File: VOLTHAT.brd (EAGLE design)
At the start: 64 x 56 mm, 25 parts, among them IC2 EUP3476SO08T, J1 DC IN

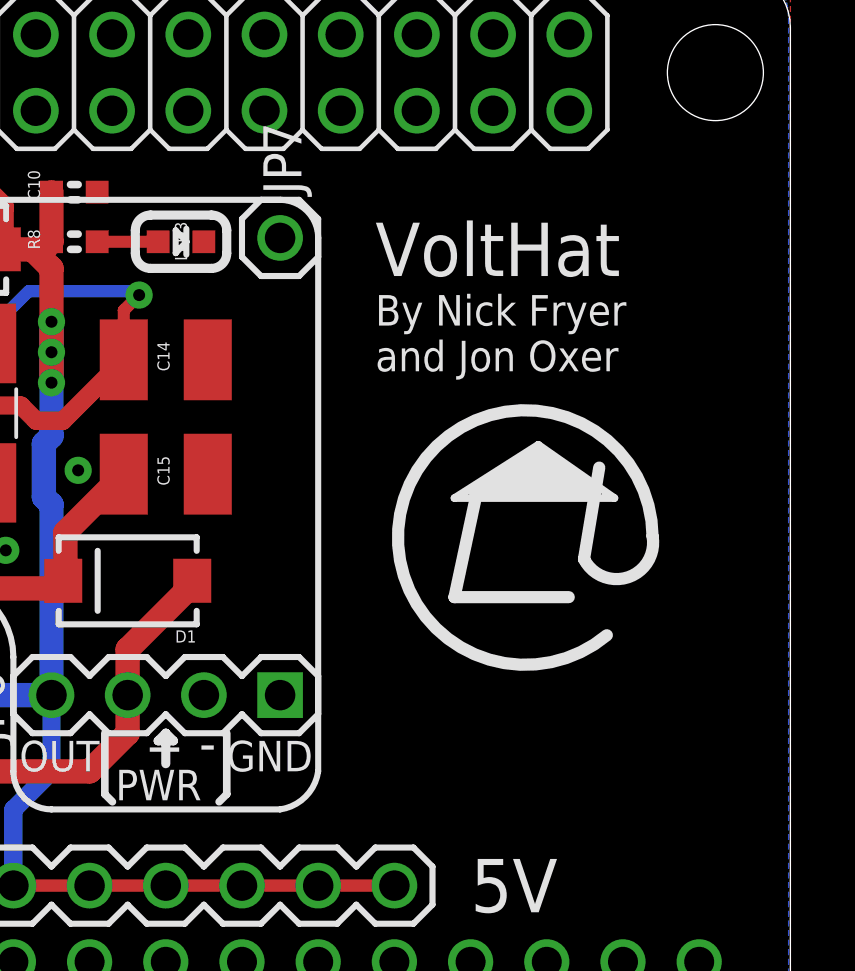
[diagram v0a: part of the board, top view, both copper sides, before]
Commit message: Added header to take power from PoE on Raspberry Pi 3 B+
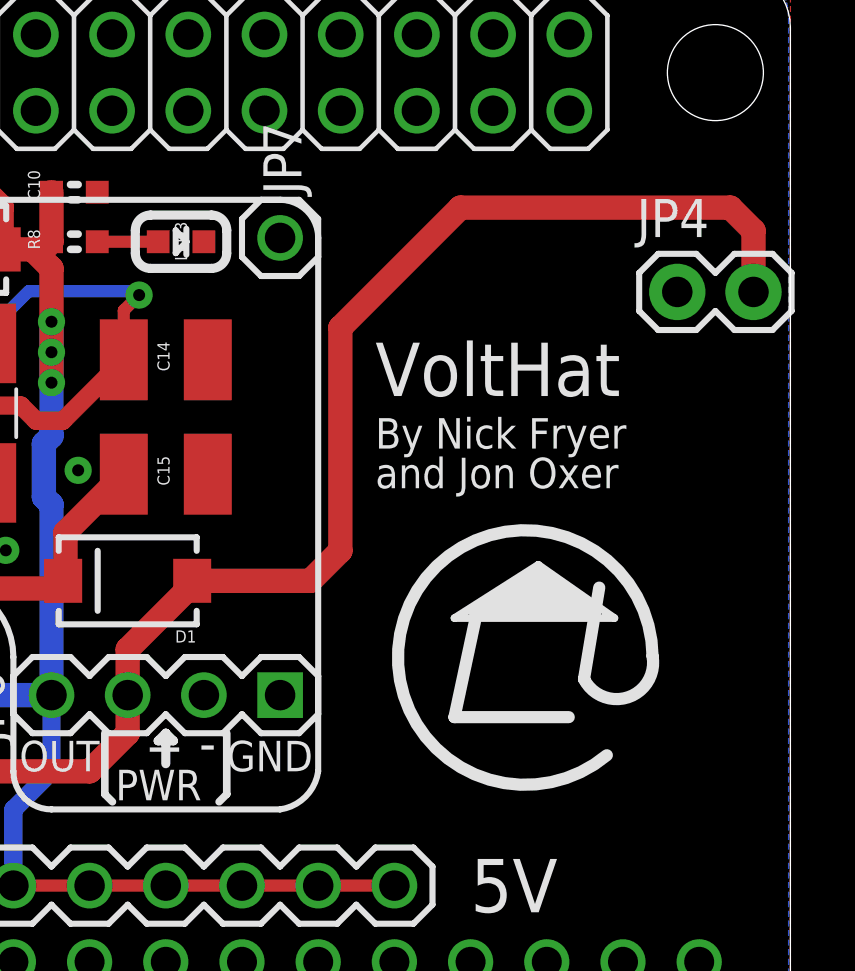
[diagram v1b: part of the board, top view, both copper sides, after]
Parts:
- added JP4: (no value), freetronics-jon:1X02
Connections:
- net GND: now also JP4.1
- net POS: now also JP4.2
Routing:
- net POS: track 49.6 -> 80.2 mm
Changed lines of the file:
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@@
 <setting verticaltext="up"/>
 </settings>
-<grid distance="0.025" unitdist="inch" unit="inch" style="lines" multiple="1" display="yes" altdistance="3.125" altunitdist="mil" altunit="mil"/>
+<grid distance="1" unitdist="mm" unit="mm" style="lines" multiple="1" display="yes" altdistance="3.125" altunitdist="mil" altunit="mil"/>
 <layers>
 <layer number="1" name="Top" color="12" fill="1" visible="yes" active="yes"/>
@@
 <text x="53.34" y="5.08" size="1.778" layer="21" font="vector" ratio="15" align="center-left">GND</text>
 <text x="5.842" y="5.08" size="1.778" layer="21" font="vector" ratio="15" align="center-left">GND</text>
-<text x="50.165" y="45.72" size="1.778" layer="21" font="vector" ratio="15">VoltHat</text>
-<text x="50.165" y="43.815" size="1.016" layer="21" font="vector" ratio="15" align="center-left">By Nick Fryer
+<text x="50.165" y="41.72" size="1.778" layer="21" font="vector" ratio="15">VoltHat</text>
+<text x="50.165" y="39.815" size="1.016" layer="21" font="vector" ratio="15" distance="30" align="center-left">By Nick Fryer
 and Jon Oxer</text>
 <hole x="3.5" y="3.5" drill="3.2"/>
@@
 <wire x1="16.891" y1="29.845" x2="17.653" y2="29.845" width="0.3048" layer="21"/>
 <text x="12.7" y="31.75" size="1.778" layer="21" font="vector" ratio="18">2.1mm</text>
-<wire x1="59.406" y1="37.048" x2="57.882" y2="33.746" width="0.4064" layer="21" curve="309.2564"/>
-<wire x1="59.406" y1="37.048" x2="57.12" y2="36.286" width="0.4064" layer="21" curve="-163.361194"/>
-<wire x1="57.12" y1="36.286" x2="57.628" y2="39.334" width="0.4064" layer="21"/>
-<wire x1="56.612" y1="35.016" x2="52.802" y2="35.016" width="0.4064" layer="21"/>
-<wire x1="52.802" y1="35.016" x2="53.564" y2="38.572" width="0.4064" layer="21"/>
-<wire x1="58.136" y1="38.318" x2="52.802" y2="38.318" width="0.254" layer="21"/>
-<wire x1="52.802" y1="38.318" x2="55.596" y2="40.096" width="0.254" layer="21"/>
-<wire x1="55.596" y1="40.096" x2="58.136" y2="38.318" width="0.254" layer="21"/>
-<wire x1="53.31" y1="38.572" x2="53.564" y2="38.572" width="0.254" layer="21"/>
-<wire x1="53.564" y1="38.572" x2="57.374" y2="38.572" width="0.254" layer="21"/>
-<wire x1="57.374" y1="38.572" x2="55.596" y2="39.842" width="0.254" layer="21"/>
-<wire x1="55.596" y1="39.842" x2="53.564" y2="38.572" width="0.254" layer="21"/>
-<wire x1="56.866" y1="38.826" x2="54.072" y2="38.826" width="0.4064" layer="21"/>
-<wire x1="54.072" y1="38.826" x2="55.596" y2="39.588" width="0.4064" layer="21"/>
-<wire x1="55.596" y1="39.588" x2="56.358" y2="39.08" width="0.4064" layer="21"/>
-<wire x1="56.358" y1="39.08" x2="55.088" y2="39.08" width="0.4064" layer="21"/>
-<wire x1="55.088" y1="39.08" x2="55.596" y2="39.334" width="0.4064" layer="21"/>
+<wire x1="59.406" y1="33.048" x2="57.882" y2="29.746" width="0.4064" layer="21" curve="309.2564"/>
+<wire x1="59.406" y1="33.048" x2="57.12" y2="32.286" width="0.4064" layer="21" curve="-163.361194"/>
+<wire x1="57.12" y1="32.286" x2="57.628" y2="35.334" width="0.4064" layer="21"/>
+<wire x1="56.612" y1="31.016" x2="52.802" y2="31.016" width="0.4064" layer="21"/>
+<wire x1="52.802" y1="31.016" x2="53.564" y2="34.572" width="0.4064" layer="21"/>
+<wire x1="58.136" y1="34.318" x2="52.802" y2="34.318" width="0.254" layer="21"/>
+<wire x1="52.802" y1="34.318" x2="55.596" y2="36.096" width="0.254" layer="21"/>
+<wire x1="55.596" y1="36.096" x2="58.136" y2="34.318" width="0.254" layer="21"/>
+<wire x1="53.31" y1="34.572" x2="53.564" y2="34.572" width="0.254" layer="21"/>
+<wire x1="53.564" y1="34.572" x2="57.374" y2="34.572" width="0.254" layer="21"/>
+<wire x1="57.374" y1="34.572" x2="55.596" y2="35.842" width="0.254" layer="21"/>
+<wire x1="55.596" y1="35.842" x2="53.564" y2="34.572" width="0.254" layer="21"/>
+<wire x1="56.866" y1="34.826" x2="54.072" y2="34.826" width="0.4064" layer="21"/>
+<wire x1="54.072" y1="34.826" x2="55.596" y2="35.588" width="0.4064" layer="21"/>
+<wire x1="55.596" y1="35.588" x2="56.358" y2="35.08" width="0.4064" layer="21"/>
+<wire x1="56.358" y1="35.08" x2="55.088" y2="35.08" width="0.4064" layer="21"/>
+<wire x1="55.088" y1="35.08" x2="55.596" y2="35.334" width="0.4064" layer="21"/>
 </plain>
 <attributes>
@@
 <attribute name="VALUE" x="41.656" y="33.909" size="0.4064" layer="27" rot="R180"/>
 </element>
+<element name="JP4" library="freetronics-jon" library_urn="urn:adsk.eagle:library:7065448" package="1X02" package3d_urn="urn:adsk.eagle:package:7066393/1" value="" x="60.23" y="45.19" smashed="yes">
+<attribute name="NAME" x="58.8838" y="47.0188" size="1.27" layer="25" ratio="10"/>
+<attribute name="VALUE" x="58.96" y="42.015" size="1.27" layer="27"/>
+</element>
 </elements>
 <signals>
@@
 <via x="40.259" y="39.243" extent="1-16" drill="0.4"/>
 <contactref element="JP3" pad="1"/>
+<contactref element="JP4" pad="1"/>
 </signal>
 <signal name="5V">
@@
 <wire x1="10.922" y1="33.02" x2="10.922" y2="38.918" width="0.8128" layer="1"/>
 <wire x1="10.922" y1="38.918" x2="7.62" y2="42.22" width="0.8128" layer="1"/>
+<contactref element="JP4" pad="2"/>
+<wire x1="44.06" y1="35.56" x2="48" y2="35.56" width="0.8128" layer="1"/>
+<wire x1="48" y1="35.56" x2="49" y2="36.56" width="0.8128" layer="1"/>
+<wire x1="49" y1="44" x2="53" y2="48" width="0.8128" layer="1"/>
+<wire x1="53" y1="48" x2="62" y2="48" width="0.8128" layer="1"/>
+<wire x1="62" y1="48" x2="62.77" y2="47.23" width="0.8128" layer="1"/>
+<wire x1="62.77" y1="47.23" x2="62.77" y2="45.19" width="0.8128" layer="1"/>
+<wire x1="49" y1="36.56" x2="49" y2="44" width="0.8128" layer="1"/>
 </signal>
 <signal name="N$204">

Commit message: Major routing for v1.0 release
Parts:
- removed JP2: M16PTH, freetronics-jon:1X16
- added JP10: OLED, freetronics-jon:1X04
- added JP9: M14PTH, freetronics-jon:1X14
- added SJ1, SJ2: (no value), freetronics-jon:SJ
- JP1: value M16PTH -> M14PTH; device freetronics-jon:1X16 -> freetronics-jon:1X14
- moved JP1 21.7 mm to (20.3, 5.08)
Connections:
- new net 3.3V: JP10.3, U$2.1
- new net N$1: JP4.1, SJ2.1
- new net N$2: JP4.2, SJ1.1
- new net SCL: JP10.2, U$2.5
- new net SDA: JP10.1, U$2.3
- net 5V: now also JP9.1, JP9.10, JP9.11, JP9.12, JP9.13, JP9.14, JP9.2, JP9.3, JP9.4, JP9.5, JP9.6, JP9.7, JP9.8, JP9.9; no longer JP1.1, JP1.10, JP1.11, JP1.12, JP1.13, JP1.14, JP1.15, JP1.16, JP1.2, JP1.3, JP1.4, JP1.5, JP1.6, JP1.7, JP1.8, JP1.9
- net GND: now also JP1.1, JP1.10, JP1.11, JP1.12, JP1.13, JP1.14, JP1.2, JP1.3, JP1.4, JP1.5, JP1.6, JP1.7, JP1.8, JP1.9, JP10.4, SJ2.2, U$2.14, U$2.20, U$2.25, U$2.30, U$2.39, U$2.9; no longer JP2.1, JP2.10, JP2.11, JP2.12, JP2.13, JP2.14, JP2.15, JP2.16, JP2.2, JP2.3, JP2.4, JP2.5, JP2.6, JP2.7, JP2.8, JP2.9, JP4.1
- net POS: now also SJ1.2; no longer JP4.2
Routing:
- net 5V: track 159.8 -> 42.0 mm, vias 3 -> 0
- net 3.3V: track 0.00 -> 42.9 mm
- net SCL: track 0.00 -> 40.2 mm
- net SDA: track 0.00 -> 36.4 mm
- net POS: track 80.2 -> 69.9 mm
- net N$2: track 0.00 -> 9.37 mm
- net N$1: track 0.00 -> 4.55 mm
- net VFEED: track 32.4 -> 28.3 mm
- added copper zone on layer 16, net 5V
- removed copper zone on layer 16, net GND
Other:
- board text added: "3V3"
- board text added: "7-28V PoE"
- board text added: "Copyright 2019 SuperHouse Automation Pty Ltd Released under the terms of the TAPR Open Hardware License: www.tapr.org/OHL"
- board text added: "I2C"
- board text added: "SCL"
- board text added: "SDA"
- board text added: "Super House"

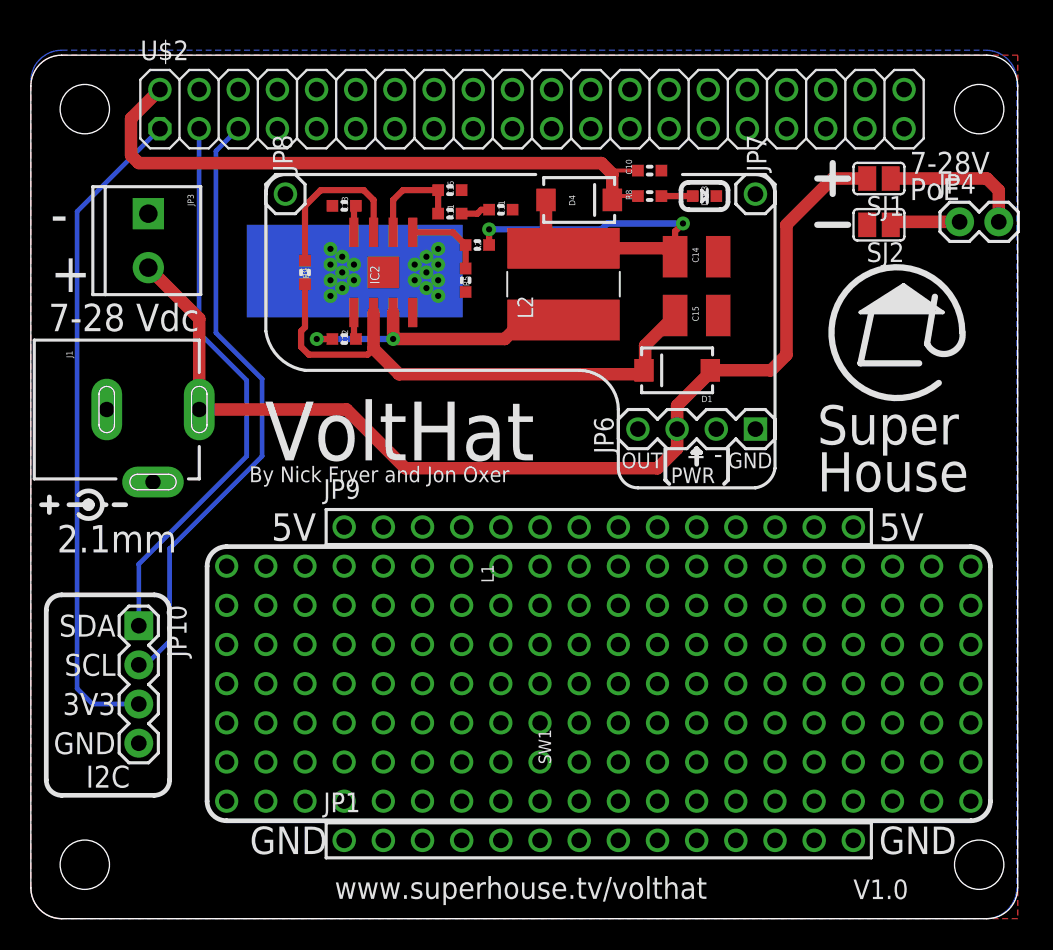
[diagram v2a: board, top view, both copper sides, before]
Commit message: Major rework with 3A regulator module for v2.0 release
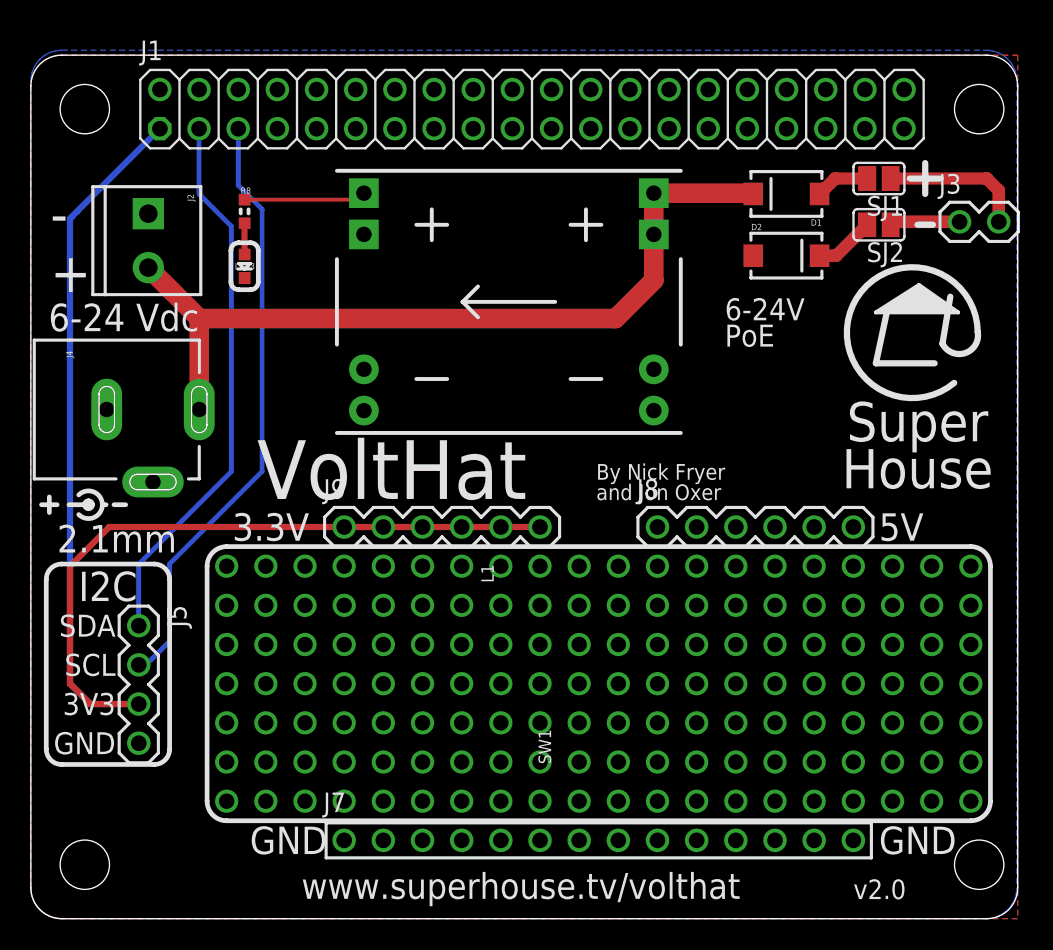
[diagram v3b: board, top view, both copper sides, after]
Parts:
- removed C10: 1uF 16V, freetronics:0603
- removed C11: 2.2nF 0603, freetronics-marc:0603
- removed C12: 10nF 50V, freetronics-marc:0603
- removed C13: 100nF, freetronics-marc:0603
- removed C14: 22uF 10V 1210 ceramic, freetronics-jon:C1210
- removed C15: 10uF 50V 1210 ceramic, freetronics-jon:C1210
- removed C16: 22pF NOT PLACED, freetronics-marc:0603
- removed D4: SK34A-LTP 3A 40V SCHOTTKY, freetronics-master-v1:SMA-DIODE
- removed IC2: EUP3476SO08T, freetronics-jon:SO08T
- removed JP10: OLED, freetronics-jon:1X04
- removed JP3: DC IN, freetronics-jon:SCREWTERMINAL-3.5MM-2
- removed JP4: (no value), freetronics-jon:1X02
- removed JP6: Pwr Header, freetronics:1X04
- removed JP7, JP8: (no value), freetronics:1X01
- removed JP9: M14PTH, freetronics-jon:1X14
- removed L2: CDRH6D38SMT, freetronics-jon:CDRH
- removed R11: 15K, freetronics-marc:0603
- removed R2: 57K 1%, freetronics-marc:0603
- removed R5: 10K 1%, freetronics-marc:0603
- removed R9: 100K, freetronics-marc:0603
- removed U$2: M40PTH, freetronics-jon:2X20
- added D2: SS56, SuperHouse-DiscreteSemi:SMA-DIODE
- added J2: DC IN, SuperHouse-Connectors:SCREWTERMINAL-3.5MM-2
- added J3: (no value), SuperHouse-Connectors:1X02-S-BELOW
- added J4: DC IN, SuperHouse-Connectors:POWER_JACK_SLOTS
- added J5: OLED, SuperHouse-Connectors:1X04
- added J8, J9: M06-PLAIN, SuperHouse-Connectors:1X06
- added VR1: DC5V3A-PTH, SuperHouse-Regulators:DC5V3A-PTH
- D1: value SK34A-LTP 3A 40V SCHOTTKY -> SS56; device freetronics-master-v1:SMA-DIODE -> SuperHouse-DiscreteSemi:SMA-DIODE
- J1: value DC IN -> M40-SOCKET-BELOW; device freetronics-jon:POWER_JACK_PTH_SLOTS -> SuperHouse-Connectors:2X20-S-BELOW
- LED3: device freetronics:LED-0603 -> SuperHouse-LEDs:LED-0603
- R8: device freetronics:0603 -> SuperHouse-DiscreteSemi:R0603
- moved LED3 30.2 mm to (13.9, 42.3), turned to 270 degrees
- moved R8 26.3 mm to (13.9, 45.9), turned to 270 degrees
- moved J1 21.4 mm to (8.37, 51.2), turned to 0 degrees
- moved D1 13.5 mm to (49.0, 47.0)
- renumbered JP1 to J7
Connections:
- removed net N$204: IC2.7, R9.1
- removed net N$205: IC2.5, R2.2, R5.2
- removed net N$206: C16.1, IC2.6, R11.2
- removed net N$207: C11.1, R11.1
- removed net N$208: C12.2, IC2.1
- removed net N$209: C13.2, IC2.8
- removed net N$210: C12.1, IC2.3, L2.1
- removed net VFEED: C14.1, D4.A, L2.2, R2.1
- removed net VIN: C15.1, D1.C, IC2.2, R9.2
- new net N$24: D1.A, SJ1.2
- new net N$25: D2.C, SJ2.2
- net 3.3V: now also J1.1, J5.3, J9.1, J9.2, J9.3, J9.4, J9.5, J9.6; no longer JP10.3, U$2.1
- net 5V: now also J1.2, J1.4, J8.1, J8.2, J8.3, J8.4, J8.5, J8.6, VR1.3A, VR1.3B; no longer C10.1, D4.C, JP6.4, JP9.1, JP9.10, JP9.11, JP9.12, JP9.13, JP9.14, JP9.2, JP9.3, JP9.4, JP9.5, JP9.6, JP9.7, JP9.8, JP9.9, U$2.2, U$2.4
- net GND: now also D2.A, J1.14, J1.20, J1.25, J1.30, J1.39, J1.6, J1.9, J2.1, J4.GND, J4.GNDBREAK, J5.4, VR1.1A, VR1.1B, VR1.4A, VR1.4B; no longer C10.2, C11.2, C13.1, C14.2, C15.2, C16.2, IC2.4, IC2.9, J1.GND, J1.GNDBREAK, JP10.4, JP3.1, JP6.1, JP6.2, JP7.1, R5.1, SJ2.2, U$2.14, U$2.20, U$2.25, U$2.30, U$2.39, U$2.6, U$2.9
- net N$1: now also J3.1; no longer JP4.1
- net N$2: now also J3.2; no longer JP4.2
- net POS: now also D1.C, J2.2, J4.PWR, VR1.2A, VR1.2B; no longer D1.A, J1.PWR, JP3.2, JP6.3, SJ1.2
- net SCL: now also J1.5, J5.2; no longer JP10.2, U$2.5
- net SDA: now also J1.3, J5.1; no longer JP10.1, U$2.3
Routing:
- net 3.3V: track 42.9 -> 87.6 mm
- net VIN: track 34.3 -> 0.00 mm
- net 5V: track 42.0 -> 7.84 mm
- net VFEED: track 28.3 -> 0.00 mm, vias 2 -> 0
- net N$210: track 19.4 -> 0.00 mm, vias 2 -> 0
- net POS: track 69.9 -> 53.3 mm
- net N$204: track 10.8 -> 0.00 mm
- net N$206: track 6.81 -> 0.00 mm
- net N$205: track 5.29 -> 0.00 mm
- net N$25: track 0.00 -> 3.92 mm
- net N$24: track 0.00 -> 3.50 mm
- net N$207: track 1.88 -> 0.00 mm
- net N$208: track 1.77 -> 0.00 mm
- net N$209: track 1.74 -> 0.00 mm
- net SCL: track 40.2 -> 39.0 mm
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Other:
- board text added: "3.3V"
- board text added: "6-24 Vdc"
- board text added: "6-24V PoE"
- board text added: "v2.0"
- board text removed: "- +"
- board text removed: "7-28 Vdc"
- board text removed: "7-28V PoE"
- board text removed: "OUT"
- board text removed: "PWR"
- board text removed: "V1.0"

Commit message: Added I2C-BREAKOUT header for v3.0 release
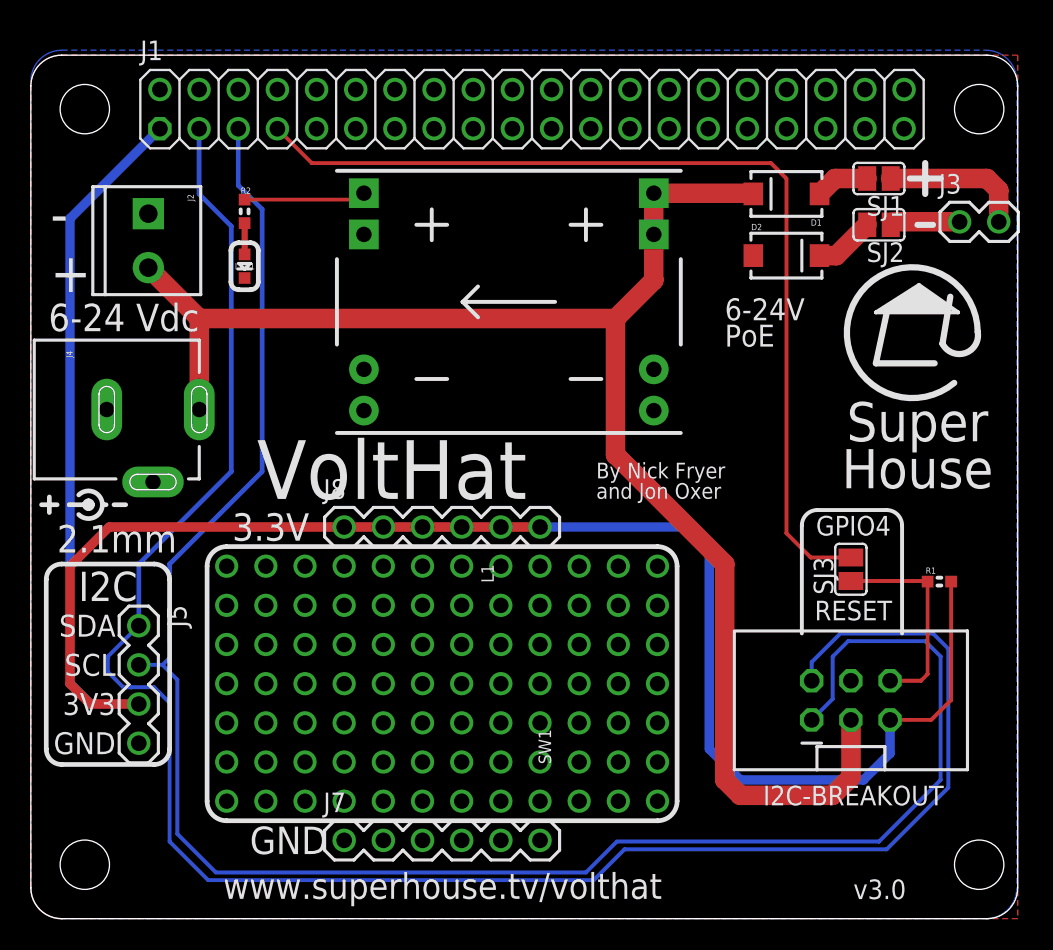
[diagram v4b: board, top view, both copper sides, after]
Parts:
- removed J9: M06-PLAIN, SuperHouse-Connectors:1X06
- added J6: I2C-BREAKOUT, SuperHouse-Connectors:2X03-SHROUDED
- added R1: 10K, SuperHouse-DiscreteSemi:R0603
- added SJ3: (no value), SuperHouse-Jumpers:SJ
- J7: value M14PTH -> M06-PLAIN; device freetronics-jon:1X14 -> SuperHouse-Connectors:1X06
- SJ1, SJ2: device freetronics-jon:SJ -> SuperHouse-Jumpers:SJ
- moved J8 20.3 mm to (20.3, 25.4)
- renumbered LED3 to LED1, R8 to R2
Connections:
- removed net POS: D1.C, J2.2, J4.PWR, VR1.2A, VR1.2B
- new net !RESET: J6.6, R1.1, SJ3.1
- new net GPIO4: J1.7, SJ3.2
- new net VIN: D1.C, J2.2, J4.PWR, J6.3, VR1.2A, VR1.2B
- net 3.3V: now also J6.5, J8.1, J8.2, J8.3, J8.4, J8.5, J8.6, R1.2; no longer J9.1, J9.2, J9.3, J9.4, J9.5, J9.6
- net 5V: no longer J8.1, J8.2, J8.3, J8.4, J8.5, J8.6
- net GND: now also J6.4; no longer J7.10, J7.11, J7.12, J7.13, J7.14, J7.7, J7.8, J7.9
- net SCL: now also J6.1
- net SDA: now also J6.2
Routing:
- net VIN: track 0.00 -> 98.8 mm
- net SDA: track 35.6 -> 127.5 mm
- net SCL: track 39.0 -> 124.5 mm
- net GPIO4: track 0.00 -> 62.2 mm
- net POS: track 53.3 -> 0.00 mm
- net 3.3V: track 87.6 -> 139.7 mm
- net !RESET: track 0.00 -> 13.6 mm
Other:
- board text added: "GPIO4"
- board text added: "I2C-BREAKOUT"
- board text added: "RESET"
- board text added: "v3.0"
- board text removed: "5V"
- board text removed: "v2.0"
